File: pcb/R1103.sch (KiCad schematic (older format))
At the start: 6 parts, among them J1 COMPUTE_MOD_1, J2 SOCKET254P-02X20

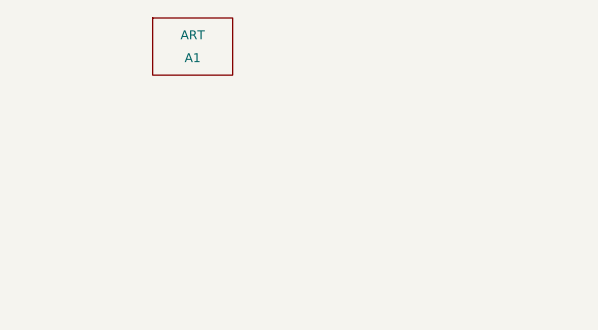
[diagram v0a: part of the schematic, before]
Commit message: adjusted layout to better fit RPi zero W
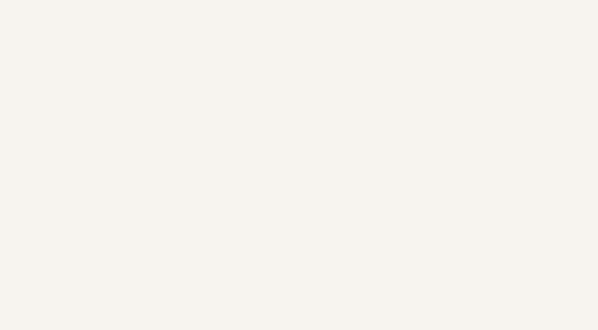
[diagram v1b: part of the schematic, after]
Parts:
- removed A1: ART, pluggee:pluggeeLabsIcon-16X8, symbol ART
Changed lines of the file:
@@
 Text Label 6150 5550 0    39   ~ 0
 SWDIO_BCM10
-$Comp
-L ART A1
-U 1 1 58E2B7DC
-P 5650 2275
-F 0 "A1" H 5650 2225 39  0000 C CNN
-F 1 "ART" H 5650 2325 39  0000 C CNN
-F 2 "pluggee:pluggeeLabsIcon-16X8" H 5650 2275 39  0001 C CNN
-F 3 "" H 5650 2275 39  0001 C CNN
-	1    5650 2275
-	1    0    0    -1
-$EndComp
 Text Label 6350 5050 2    39   ~ 0
 SCK
